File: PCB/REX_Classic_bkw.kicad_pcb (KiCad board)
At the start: 2 copper layers, 38 x 16.6 mm, 12 parts, among them J1 Tandy_100_102_200_option_rom, J2 JTAG, J3 PRG, U1 XCR3064XL-VQ44, U2 29F800BB, U3 LP2980-3.3

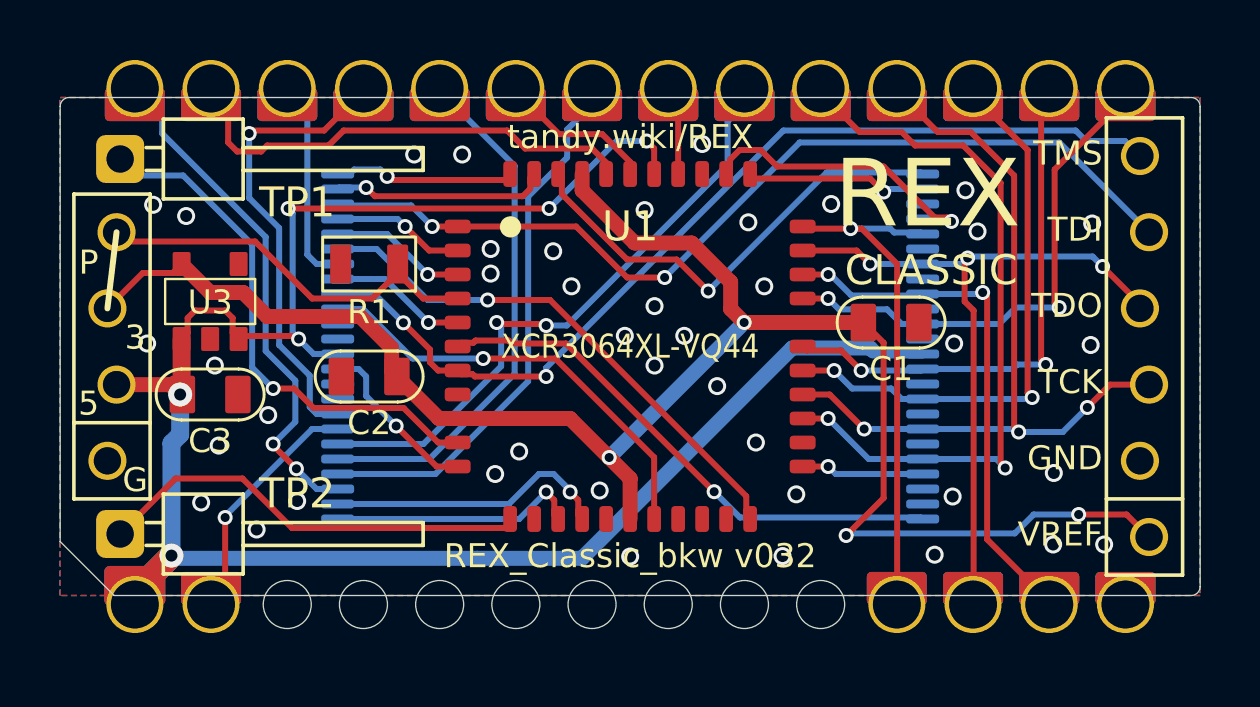
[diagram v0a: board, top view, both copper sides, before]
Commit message: housing component, fillet tracks, molex datasheets corrections
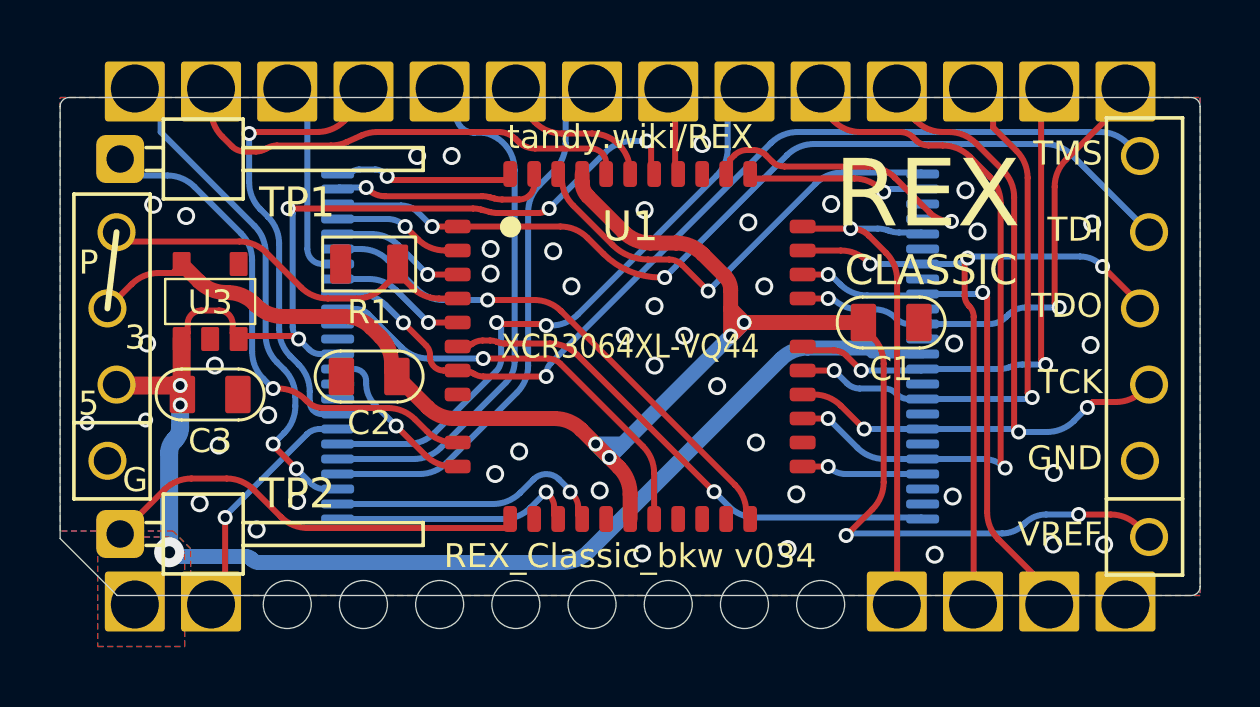
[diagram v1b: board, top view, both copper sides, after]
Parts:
- added N1: Molex78802_PCB_28 Carrier, 000_LOCAL:Housing_Molex78802_PCB_28, F.Cu at (137.2, 99.2)
- C1, C2, C3: value 1uF -> 1u
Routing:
- net +5V: track 66.4 -> 62.9 mm, vias 6 -> 7
- net +3V3: track 60.0 -> 59.0 mm, vias 4 -> 6
- net /~{OE_BUS}: track 2.45 -> 2.99 mm
- net /A10: track 7.56 -> 8.07 mm
- net GND: vias 42 -> 44
- added copper zone on B.Cu, net +5V
- added copper zone on F.Cu, net +5V
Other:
- outline, holes or cut-outs redrawn
